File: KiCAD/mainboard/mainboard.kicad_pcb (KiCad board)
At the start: 10 copper layers, 156 parts, among them IC14 SN74AUP1G06DCKR, IC3 SN74AUP1G06DCKR, IC4 SN74AUP1G07DCKR, IC5 SN74AUP1G07DCKR, IC6 SN74AUP1G06DCKR, J1 AXT550124, J10 Conn_01x05_Pin, J100 AHDF15A-KG-TAXB, J14 Conn_01x04_Pin, J2 Conn_01x07_Pin, J29 Conn_01x04_Pin, J3 Conn_02x05_Odd_Even, J30 Conn_01x08_Pin, J31 Conn_01x08_Pin, J4 Conn_01x05_Pin, U12 ECS-2520MV-xxx-xx, U13 MX25L3233FM2, U16 DLPC1438ZEZ, U22 TXS0102DCU, U24 DLPA2005ERSLT, U26 TPS54340DDA, U37 TXS0102DCU, U39 TPS62260DDCT, U7 SN74AUP1G06DCKR

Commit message: BGA layout cont
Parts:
- removed the J10 at (134.7, 89.9)
- removed REF**: RESC2012X60N, tp_library:RESC2012X60N
- removed REF**: STA_RMCF0805_STP, tp_library:STA_RMCF0805_STP-M
- removed REF**: RES_R-070RL_VIS, tp_library:RES_R-070RL_VIS-M
- removed REF**: CAPC2012X70, tp_library:CAPC2012X70
- removed REF**: RES_ERJP06_PAN, tp_library:RES_ERJP06_PAN-M
- removed REF**: RES_CRCW_0805, tp_library:RES_CRCW_0805-M
- removed REF**: BLM15P_FBD, tp_library:BLM15P_FBD-M
- removed REF**: RES_RM10_CCE, tp_library:RES_RM10_CCE-M
- removed REF**: LED_SML-LX1206SIC-TR_LUM, tp_library:LED_SML-LX1206SIC-TR_LUM-M
- removed REF**: RES_RMCF0805_STP, tp_library:RES_RMCF0805_STP-M
- added R172: 30.1, tp_library:RESC2012X60N, F.Cu at (192.5, 34.5)
- added R173: 30.1, tp_library:RESC2012X60N, F.Cu at (11.1, 44.2)
- added R18: 30.1, tp_library:RESC2012X60N, F.Cu at (221.1, 41.1)
- added R43: 30.1, tp_library:RESC2012X60N, F.Cu at (206.3, 46.5)
- added R74: 30.1, tp_library:RESC2012X60N, F.Cu at (89.3, 11.4)
- added R75: 30.1, tp_library:RESC2012X60N, F.Cu at (89.6, 8.35)
- added R76: 30.1, tp_library:RESC2012X60N, F.Cu at (89.3, 14.7)
- added R77: 30.1, tp_library:RESC2012X60N, F.Cu at (89.6, 17.6)
- added R83: 30.1, tp_library:RESC2012X60N, F.Cu at (15.2, 0.96)
- added TP14: TestPoint, TestPoint:TestPoint_Pad_D1.5mm, F.Cu at (5.66, 4.83)
- added TP2: TestPoint, TestPoint:TestPoint_Pad_D1.5mm, F.Cu at (11.2, 1.27)
- added TP22: TestPoint, TestPoint:TestPoint_Pad_D1.5mm, F.Cu at (11.2, 4.83)
- added TP3: TestPoint, TestPoint:TestPoint_Pad_D1.5mm, F.Cu at (5.66, 1.27)
- added TP35: TestPoint, TestPoint:TestPoint_Pad_D1.5mm, F.Cu at (11.2, 8.38)
- added TP36: TestPoint, TestPoint:TestPoint_Pad_D1.5mm, F.Cu at (11.2, 11.9)
- added TP38: TestPoint, TestPoint:TestPoint_Pad_D1.5mm, F.Cu at (11.2, 15.5)
- moved C168 256.0 mm to (20.1, 103.9)
- moved C21 256.0 mm to (20.1, 93.9)
- moved C211 256.0 mm to (20.1, 106.4)
- moved C212 256.0 mm to (20.1, 108.9)
- moved C22 256.0 mm to (20.1, 96.4)
- moved C30 256.0 mm to (20.1, 98.9)
- moved C31 256.0 mm to (20.1, 101.4)
- moved J14 238.5 mm to (14.6, 157.9)
- moved R84 238.5 mm to (21.2, 160.2)
- moved C1 226.7 mm to (34.9, 162.1)
- moved C24 226.7 mm to (34.9, 170.3)
- moved C82 226.7 mm to (34.9, 178.4)
- moved C96 226.7 mm to (34.9, 186.6)
- moved D12 226.7 mm to (57.5, 159.4)
- moved R3 226.7 mm to (58.9, 165.9)
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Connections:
- net Net-(U16-PDM_CVS__TE) renamed /DLPC1438_Interface/PDM_CVS_TE
- U16 pad R10: /DLPC1438_Interface/IIC1_SCL -> /DLPC1438_Interface/IIC1_SDA_1p8
- U16 pad R11: /DLPC1438_Interface/IIC1_SDA -> /DLPC1438_Interface/IIC1_SCL_1p8

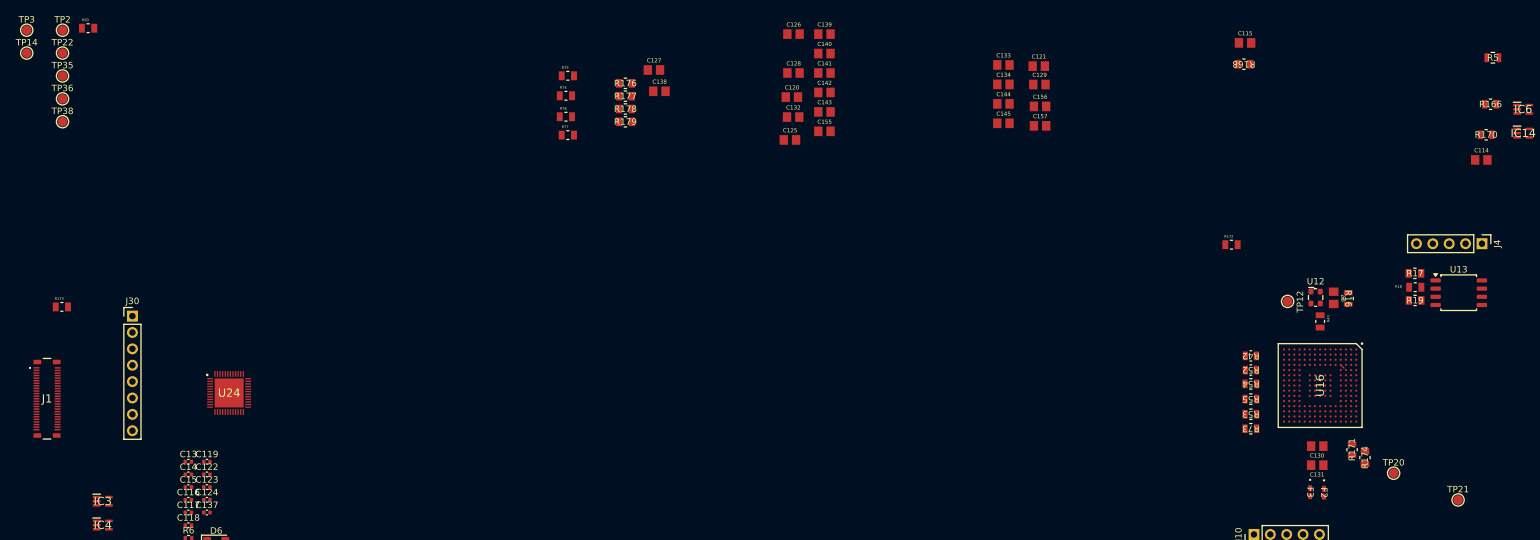
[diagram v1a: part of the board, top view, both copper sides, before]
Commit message: decoupling caps and pullup down resistors layout
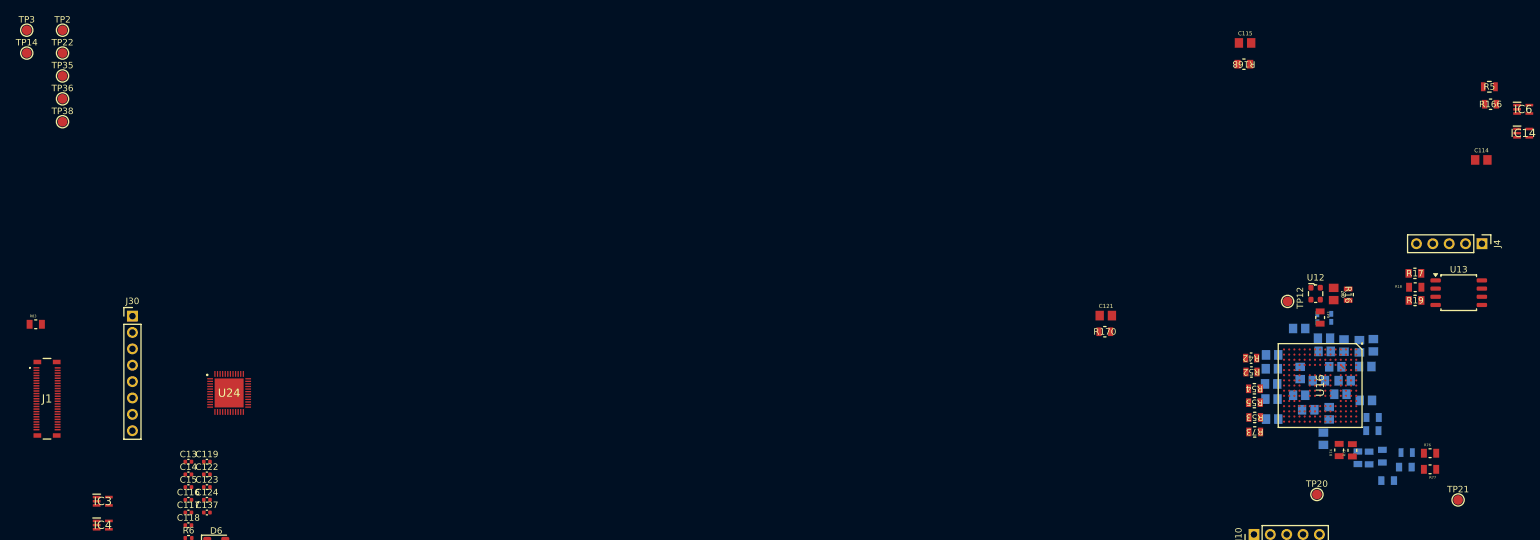
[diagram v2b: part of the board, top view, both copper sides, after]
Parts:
- C120, C125, C126, C127, C128, C129, C130, C131, C132, C133, C134, C138, C139, C140, C141, C142, C143, C144, C145, C155, C156, C157, F2, F3, R171, R172, R173, R174, R176, R177, R178, R179: moved to B.Cu
- moved R173 204.2 mm to (214.4, 63.4), turned to 180 degrees
- moved R76 143.9 mm to (223.3, 66.9)
- moved R77 143.5 mm to (223.3, 69.4), turned to 180 degrees
- moved R75 134.9 mm to (211.3, 66.5), turned to 90 degrees
- moved R176 134.8 mm to (219.5, 69.0), turned to 180 degrees
- moved R74 131.9 mm to (209.2, 66.4), turned to 90 degrees
- moved R179 130.7 mm to (216.8, 71.2), turned to 180 degrees
- moved R177 130.0 mm to (215.9, 67.3), turned to 90 degrees
- moved R178 127.4 mm to (213.9, 67.7), turned to 90 degrees
- moved C138 119.6 mm to (213.4, 58.7), turned to 180 degrees
- moved C127 117.5 mm to (212.4, 50.3), turned to -90 degrees
- moved C126 102.1 mm to (214.6, 50.1), turned to -90 degrees
- moved C139 97.0 mm to (210.1, 55.6), turned to 180 degrees
- moved C140 95.9 mm to (209.4, 57.8), turned to 180 degrees
- moved C125 95.9 mm to (213.3, 53.5), turned to 180 degrees
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
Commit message: i hope this doesn't mess things
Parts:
- R166, R168: moved to B.Cu
- moved J3 193.7 mm to (283.4, 5.06), turned to -90 degrees
- moved J2 185.5 mm to (248.2, 4.40), turned to -90 degrees
- moved TP7 183.7 mm to (287.6, 14.2)
- moved R163 177.2 mm to (280.4, 12.2), turned to 90 degrees
- moved R165 176.4 mm to (288.8, 19.4), turned to 90 degrees
- moved C112 174.5 mm to (248.3, 8.65), turned to 90 degrees
- moved R164 170.9 mm to (232.6, 8.75), turned to 90 degrees
- moved J31 122.0 mm to (278.7, 66.7)
- moved U22 74.2 mm to (206.1, 51.5)
- moved D7 72.8 mm to (215.0, 4.27), turned to 90 degrees
- moved C171 72.1 mm to (205.9, 54.3), turned to 180 degrees
- moved U7 71.9 mm to (214.2, 13.6), turned to 90 degrees
- moved R7 71.1 mm to (215.1, 9.70), turned to 90 degrees
- moved R168 70.0 mm to (263.0, 20.6), turned to -90 degrees
- moved R92 69.9 mm to (209.3, 57.4), turned to 90 degrees
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
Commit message: pcb update, some vias are violating DRC
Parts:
- C115: moved to B.Cu
- moved C115 57.0 mm to (261.1, 23.4), turned to 180 degrees
- moved R179 20.7 mm to (229.6, 59.0), turned to 90 degrees
- moved J100 18.2 mm to (42.0, 127.5)
- moved R77 9.80 mm to (247.7, 49.0)
- moved R76 9.64 mm to (247.7, 46.9)
- moved R176 7.03 mm to (245.9, 51.1), turned to 0 degrees
- moved R178 6.52 mm to (240.6, 50.4), turned to -90 degrees
- moved R177 6.26 mm to (242.8, 50.5)
- moved R171 3.78 mm to (249.9, 48.4), turned to 180 degrees
- moved C114 3.50 mm to (209.0, 17.1)
- moved C121 3.50 mm to (209.6, 32.0)
- moved C170 3.50 mm to (209.7, 48.2)
- moved C171 3.50 mm to (209.4, 54.3)
- moved D7 3.50 mm to (218.5, 4.28)
- moved R166 3.50 mm to (209.2, 21.7)
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- renumbered IC14 to U14, IC6 to U5
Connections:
- R176 pad 1: /DLPC1438_Interface/SPI1_CLK -> /DLPC1438_Interface/GPIO_1
- R178 pad 1: /DLPC1438_Interface/SPI1_MOSI -> /DLPC1438_Interface/GPIO_2
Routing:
- net GND: track 0.00 -> 31.8 mm, vias 0 -> 49
- net P1P8V_DLPC: track 0.71 -> 6.54 mm, vias 0 -> 5
- net /DLPC1438_Interface/VSS_PLL: track 0.00 -> 4.88 mm
- net /DLPC1438_Interface/VDD_PLL: track 0.00 -> 4.77 mm
- net P1P1V: track 0.00 -> 4.15 mm, vias 0 -> 3
- net /DLPC1438_Interface/SPI1_MISO: track 0.00 -> 2.86 mm
- net /DLPC1438_Interface/SPI0_MISO: track 0.00 -> 2.60 mm
- net /DLPC1438_Interface/SPI0_5V: track 0.00 -> 2.55 mm
- net /DLPA2005_Interface/LED_SEL_1: track 0.00 -> 2.22 mm
- net /DLPC1438_Interface/DLPC_FLSH_PROG: track 0.00 -> 1.60 mm, vias 0 -> 1
- net /DLPC1438_Interface/SPI0_MOSI: track 0.00 -> 1.40 mm, vias 0 -> 1
- net P3P3V_SB: track 0.00 -> 1.30 mm, vias 0 -> 1
- net /DLPC1438_Interface/SPI0_CLK: track 0.00 -> 1.17 mm, vias 0 -> 1
- net /DLPC1438_Interface/DLPC_LED_SEL_1: track 0.00 -> 1.07 mm, vias 0 -> 1
- net P3P3V: track 0.00 -> 0.71 mm

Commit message: more layout stuff
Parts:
- added D5: SML-LX1206SIC-TR, tp_library:LED_SML-LX1206SIC-TR_LUM-M, F.Cu at (187.3, 26.7)
- C108, C115, C120, C125, C126, C127, C128, C129, C130, C131, C132, C133, C134, C138, C139, C140, C141, C142, C143, C144, C145, C155, C156, C157, C170, C171, C238, C239, C7: footprint tp_library:CAPC2012X70 -> tp_library:CAP_CL05_SAM
- C112, C114, C121: footprint tp_library:CAPC2012X70 -> tp_library:CAP_CL05_SAM; moved to B.Cu
- C116, C122, C123, C124, C13, C137, C14, C15: footprint Capacitor_SMD:C_0402_1005Metric -> tp_library:CAP_CL05_SAM
- R164, R170: moved to B.Cu
- moved C109 113.7 mm to (146.2, 132.4)
- moved C110 113.7 mm to (146.2, 134.9)
- moved C19 113.7 mm to (146.2, 119.8)
- moved C25 113.7 mm to (146.2, 122.3)
- moved C26 113.7 mm to (146.2, 124.8)
- moved C3 113.7 mm to (146.2, 117.3)
- moved C41 113.7 mm to (146.2, 127.4)
- moved J14 113.7 mm to (118.9, 112.5)
- moved R117 113.7 mm to (162.3, 117.6)
- moved R95 113.7 mm to (163.7, 123.6)
- moved C1 113.7 mm to (139.2, 116.8)
- moved C2 113.7 mm to (146.2, 114.8)
- moved C24 113.7 mm to (139.2, 124.9)
- moved C51 113.7 mm to (146.2, 129.9)
- moved C71 113.7 mm to (150.7, 115.1)
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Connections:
- R176 pad 1: /DLPC1438_Interface/GPIO_1 -> /DLPC1438_Interface/SPI1_CLK
- R178 pad 1: /DLPC1438_Interface/GPIO_2 -> /DLPC1438_Interface/SPI1_MOSI
- R5 pad 1: P3P3V -> Net-(D5-Pad1)
- U16 pad F15: /DLPC1438_Interface/ACT_SYNC -> unconnected-(U16-GPIO_07-PadF15)
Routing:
- net GND: track 31.8 -> 73.7 mm, vias 49 -> 92
- net /DLPC1438_Interface/SPI0_MOSI: track 1.40 -> 18.9 mm, vias 1 -> 2
- net /DLPC1438_Interface/SPI0_CSZ0: track 0.00 -> 12.9 mm
- net P1P8V_DLPC: track 6.54 -> 15.8 mm, vias 5 -> 12
- net /DLPC1438_Interface/IIC1_SDA_1p8: track 0.00 -> 7.51 mm, vias 0 -> 1
- net /DLPC1438_Interface/IIC1_SCL_1p8: track 0.00 -> 7.10 mm, vias 0 -> 1
- net /DLPC1438_Interface/VOSC: track 0.00 -> 6.96 mm, vias 0 -> 1
- net P3P3V_SB: track 1.30 -> 6.51 mm, vias 1 -> 5
- net /DLPC1438_Interface/OSC_OUT: track 0.00 -> 4.00 mm
- net /DLPC1438_Interface/JTAG_TRSTZ: track 0.00 -> 3.20 mm
- net /DLPC1438_Interface/RSTZ_LED: track 0.00 -> 3.04 mm
- net Net-(D5-Pad1): track 0.00 -> 2.51 mm
- net /DLPC1438_Interface/SPI0_MISO_T: track 0.00 -> 2.30 mm
- net /DLPC1438_Interface/RSTZ_LED_OUT: track 0.00 -> 2.12 mm
- net P3P3V: track 0.71 -> 2.73 mm, vias 0 -> 2
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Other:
- board outline added: 190.9 x 151.2 mm

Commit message: layout
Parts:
- moved J14 147.1 mm to (265.7, 102.5)
- moved J30 123.3 mm to (204.4, 128.3), turned to 90 degrees
- moved U24 122.9 mm to (230.0, 107.0)
- moved J1 106.3 mm to (172.7, 18.4), turned to 90 degrees
- moved J100 106.0 mm to (166.9, 60.6), turned to 90 degrees
- moved C108 104.5 mm to (152.8, 91.5)
- moved C238 104.5 mm to (158.8, 90.0)
- moved C239 104.5 mm to (158.8, 93.0)
- moved R156 104.5 mm to (163.6, 82.0)
- moved R157 104.5 mm to (163.6, 85.0)
- moved R8 104.5 mm to (157.6, 84.8)
- moved R158 104.5 mm to (151.9, 88.3)
- moved J29 104.5 mm to (171.5, 83.5)
- moved R155 104.5 mm to (151.9, 85.3)
- moved U37 104.5 mm to (165.8, 90.8)
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
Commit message: i hope no layout changes have been made before this pull
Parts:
- moved C155 0.40 mm to (218.5, 57.9)
- moved C139 0.33 mm to (220.8, 52.4)
- moved C141 0.14 mm to (214.8, 56.2)

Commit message: more layout
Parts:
- moved J100 21.5 mm to (187.2, 53.7), turned to -90 degrees
- moved R170 14.5 mm to (194.9, 34.5)
- moved U14 14.5 mm to (195.2, 34.5)
- moved U22 14.2 mm to (197.2, 76.8)
- moved C171 14.2 mm to (197.2, 79.9)
- moved R92 14.2 mm to (199.7, 82.5)
- moved C170 14.2 mm to (197.0, 73.7)
- moved C121 11.1 mm to (190.9, 31.9)
- moved C126 3.68 mm to (221.3, 47.6)
- moved C115 3.46 mm to (240.5, 33.8)
- moved R17 3.46 mm to (231.3, 35.5)
- moved R18 3.46 mm to (231.1, 37.7)
- moved R19 3.46 mm to (231.1, 39.8)
- moved U13 3.46 mm to (237.9, 38.6)
- moved J4 3.46 mm to (242.1, 26.3)
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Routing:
- net /DLPC1438_Interface/DMD_HS_WDATAB_N: track 0.00 -> 49.8 mm
- net /DLPC1438_Interface/DMD_HS_WDATAC_N: track 0.00 -> 49.3 mm
- net /DLPC1438_Interface/DMD_HS_WDATAH_N: track 0.00 -> 49.2 mm
- net /DLPC1438_Interface/DMD_HS_WDATAD_N: track 0.00 -> 49.2 mm
- net /DLPC1438_Interface/DMD_HS_WDATAB_P: track 0.00 -> 48.4 mm
- net /DLPC1438_Interface/DMD_HS_WDATAF_N: track 0.00 -> 48.2 mm
- net /DLPC1438_Interface/DMD_HS_CLK_N: track 0.00 -> 48.1 mm
- net /DLPC1438_Interface/DMD_HS_WDATAC_P: track 0.00 -> 48.0 mm
- net /DLPC1438_Interface/DMD_HS_WDATAE_N: track 0.00 -> 48.0 mm
- net /DLPC1438_Interface/DMD_HS_WDATAH_P: track 0.00 -> 47.9 mm
- net /DLPC1438_Interface/DMD_HS_WDATAG_P: track 0.00 -> 47.6 mm
- net /DLPC1438_Interface/DMD_HS_CLK_P: track 0.00 -> 47.4 mm
- net /DLPC1438_Interface/DMD_HS_WDATAE_P: track 0.00 -> 47.3 mm
- net /DLPC1438_Interface/DMD_HS_WDATAA_N: track 0.00 -> 47.3 mm
- net /DLPC1438_Interface/DMD_HS_WDATAD_P: track 0.00 -> 47.3 mm
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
